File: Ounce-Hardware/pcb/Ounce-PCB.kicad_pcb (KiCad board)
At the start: 2 copper layers, 135 x 61 mm, 5 parts, among them U1 RaspberryPi_Pico2_W, U2 RaspberryPi_Pico, U3 RaspberryPi_Pico, U4 RaspberryPi_Pico, U5 RaspberryPi_Pico

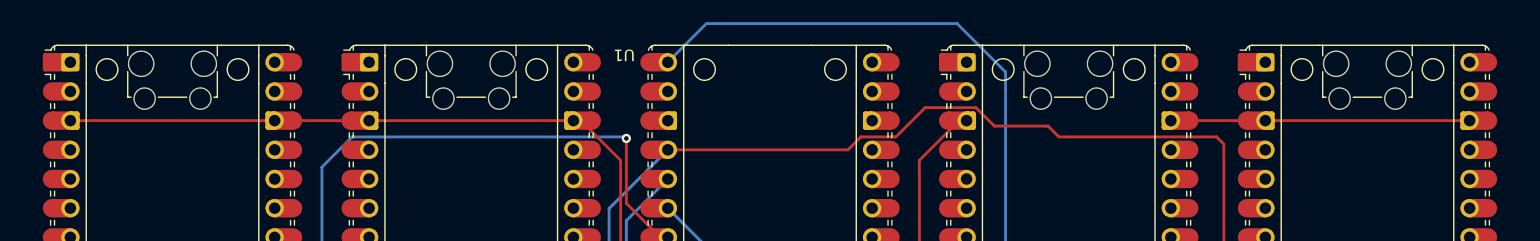
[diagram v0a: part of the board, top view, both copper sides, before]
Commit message: Revert the partial ground crossings
Three of the five could be routed and two could not, which leaves the ground
inconsistent - some modules bridged in copper, others relying on the Pico
internally. Removed all three so the board is uniform again and is your routing
as saved, plus the duplicate via fix.

Back to 5 unconnected, all ground, all of them the pin 3 to pin 38 links inside
each module.

Co-Authored-By: Claude Opus 5 <noreply@anthropic.com>
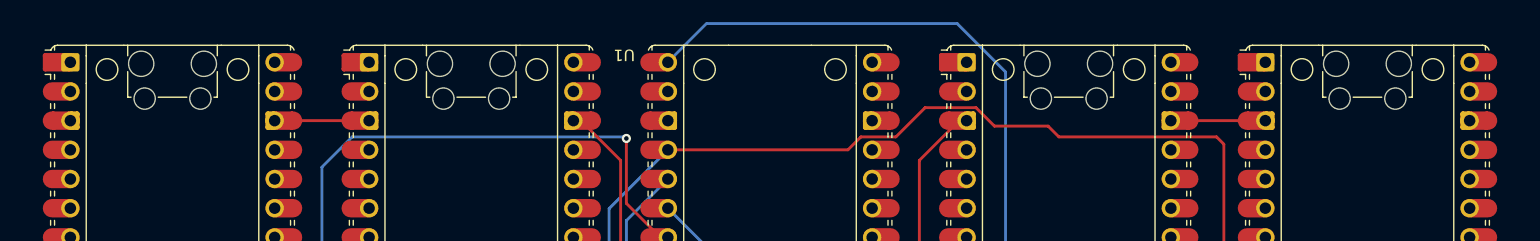
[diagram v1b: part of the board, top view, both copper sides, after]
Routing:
- net GND: track 156.3 -> 103.0 mm
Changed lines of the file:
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@@
-	)
-	(segment
-		(start 89.11 80.95)
-		(end 106.89 80.95)
-		(width 0.25)
-		(layer "F.Cu")
-		(net "GND")
 	)
 	(segment
@@
 	)
 	(segment
-		(start 115.11 80.95)
-		(end 132.89 80.95)
-		(width 0.25)
-		(layer "F.Cu")
-		(net "GND")
-	)
-	(segment
 		(start 163 115.59099)
 		(end 159.54099 119.05)
@@
 		(width 0.25)
 		(layer "F.Cu")
-		(net "GND")
-	)
-	(segment
-		(start 193.11 80.95)
-		(end 210.89 80.95)
-		(width 0.25)
-		(layer "F.Cu")

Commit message: Add three of the five ground crossings
U2, U3 and U5 now have copper from pin 3 to pin 38, so ground no longer relies
on those three modules bridging internally. Copper ground networks drop from 4
islands plus 2 orphans to 3 islands, and DRC unconnected from 5 to 2.

U1 and U4 could not be added. Their interiors are full: signal traces on both
layers plus 19 copper keepouts per module from the footprint, several of them
mid-body rather than just at the antenna. A grid search at 0.5mm with 0.45mm
clearance found no path on F.Cu or B.Cu for either. The straight crossing hits
SCK and CS1 on the front and MISO1 and MISO2 on the back; a dogleg through the
one clear lane runs into a keepout at y 81.55..85.75.

So ground still depends on U1 and U4 bridging pin 3 to pin 38 internally, which
is sound with every module seated - the case that already holds here - but is
not copper. Fixing it properly means moving signal routing, not adding a trace.

Co-Authored-By: Claude Opus 5 <noreply@anthropic.com>
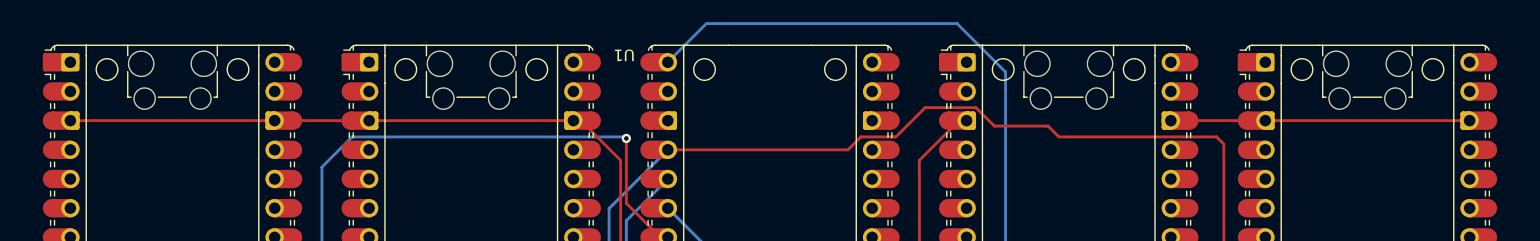
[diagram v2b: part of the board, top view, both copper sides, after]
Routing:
- net GND: track 103.0 -> 156.3 mm
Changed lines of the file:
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@@
+	)
+	(segment
+		(start 89.11 80.95)
+		(end 106.89 80.95)
+		(width 0.25)
+		(layer "F.Cu")
+		(net "GND")
 	)
 	(segment
@@
 	)
 	(segment
+		(start 115.11 80.95)
+		(end 132.89 80.95)
+		(width 0.25)
+		(layer "F.Cu")
+		(net "GND")
+	)
+	(segment
 		(start 163 115.59099)
 		(end 159.54099 119.05)
@@
 		(width 0.25)
 		(layer "F.Cu")
+		(net "GND")
+	)
+	(segment
+		(start 193.11 80.95)
+		(end 210.89 80.95)
+		(width 0.25)
+		(layer "F.Cu")
